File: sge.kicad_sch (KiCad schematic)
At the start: 27 parts, among them IC6 315-5660

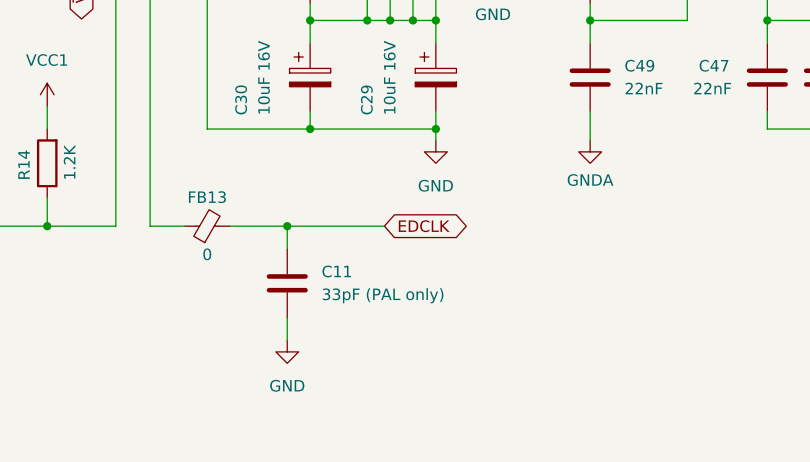
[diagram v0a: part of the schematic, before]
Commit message: Remove PAL-only designation from C11 (issue #10).
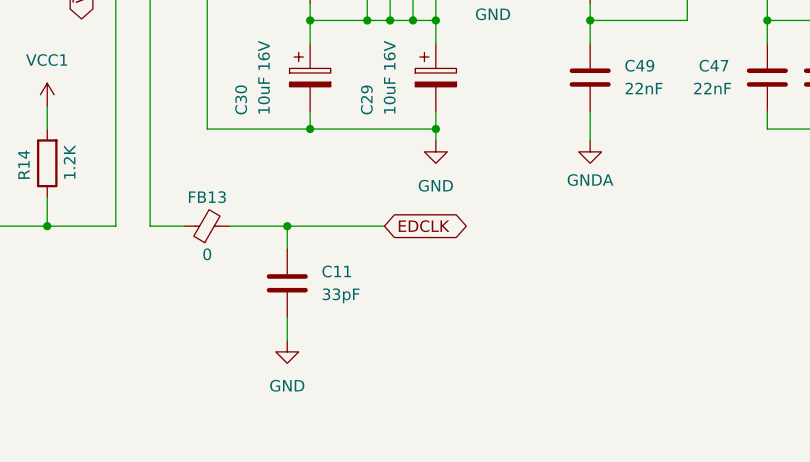
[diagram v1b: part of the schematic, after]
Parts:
- C11: value 33pF (PAL only) -> 33pF
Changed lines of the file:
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@@
 		(fields_autoplaced yes)
 		(property "Reference" "C11"
-			(at 265.43 259.715 0)
+			(at 265.43 259.7149 0)
 			(effects
 				(font
@@
 			)
 		)
-		(property "Value" "33pF (PAL only)"
-			(at 265.43 262.255 0)
+		(property "Value" "33pF"
+			(at 265.43 262.2549 0)
 			(effects
 				(font

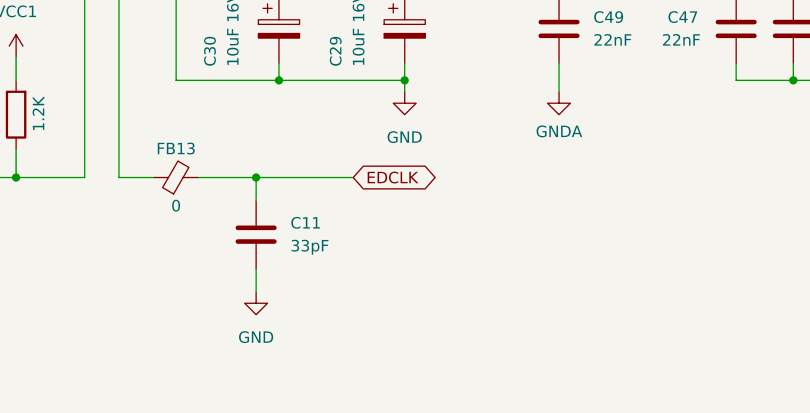
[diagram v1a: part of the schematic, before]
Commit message: Add note for C11 (issue #10).
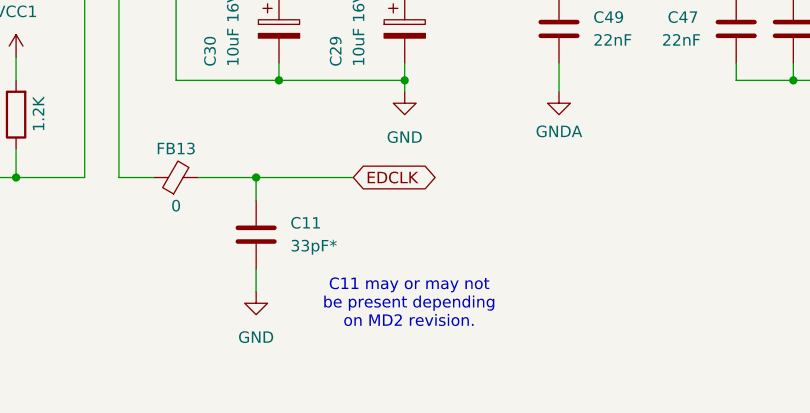
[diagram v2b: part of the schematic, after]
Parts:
- C11: value 33pF -> 33pF*
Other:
- note added: "C11 may or may not be present depending on MD2 revision."
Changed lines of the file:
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@@
 		)
 	)
+	(text "C11 may or may not\nbe present depending\non MD2 revision."
+		(exclude_from_sim no)
+		(at 278.638 268.732 0)
+		(effects
+			(font
+				(size 1.27 1.27)
+			)
+		)
+	)
 	(junction
 		(at 292.1 222.25)
@@
 			)
 		)
-		(property "Value" "33pF"
+		(property "Value" "33pF*"
 			(at 265.43 262.2549 0)
 			(effects
